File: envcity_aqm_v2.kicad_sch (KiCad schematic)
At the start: 127 parts, among them IC1 DS1307ZN+, IC2 DMMT5401-7F, IC3 DMMT5401-7F, IC4 DMMT5401-7-F, IC6 ESP32-S2-SOLO-N4R2, J1 USB_B_Micro, J12 Conn_01x06_Male, J13 Conn_01x06_Male, J14 Conn_01x08_Pin, J15 Conn_01x02_Male, J16 Conn_01x02_Male, J2 Screw_Terminal_01x02, J3 Screw_Terminal_01x02, J6 Conn_01x04_Male, J7 Conn_01x06_Pin, J8 503398-1892, Q1 DMG2301L / DMP2045U, Q2 DMG2301L / DMP2045U, Q3 DMG2301L, Q4 DMG2301L, Q5 DMG2301L / DMP2045U, Q6 DMG2301L, Q7 DMN10H220L, Q8 DMN10H220L, SW1 BOOT, SW1 RESET, U1 TP4056, U10 RFM95W-915S2, U11 ADS1115IDGS, U2 USBLC6-2SC6, U3 MT3608, U5 LM2596S-5, U6 AP2112K-3.3, U7 DHT11, U8 AP2112K-3.3, U9 74HC4067DB, Y2 AB26TRB

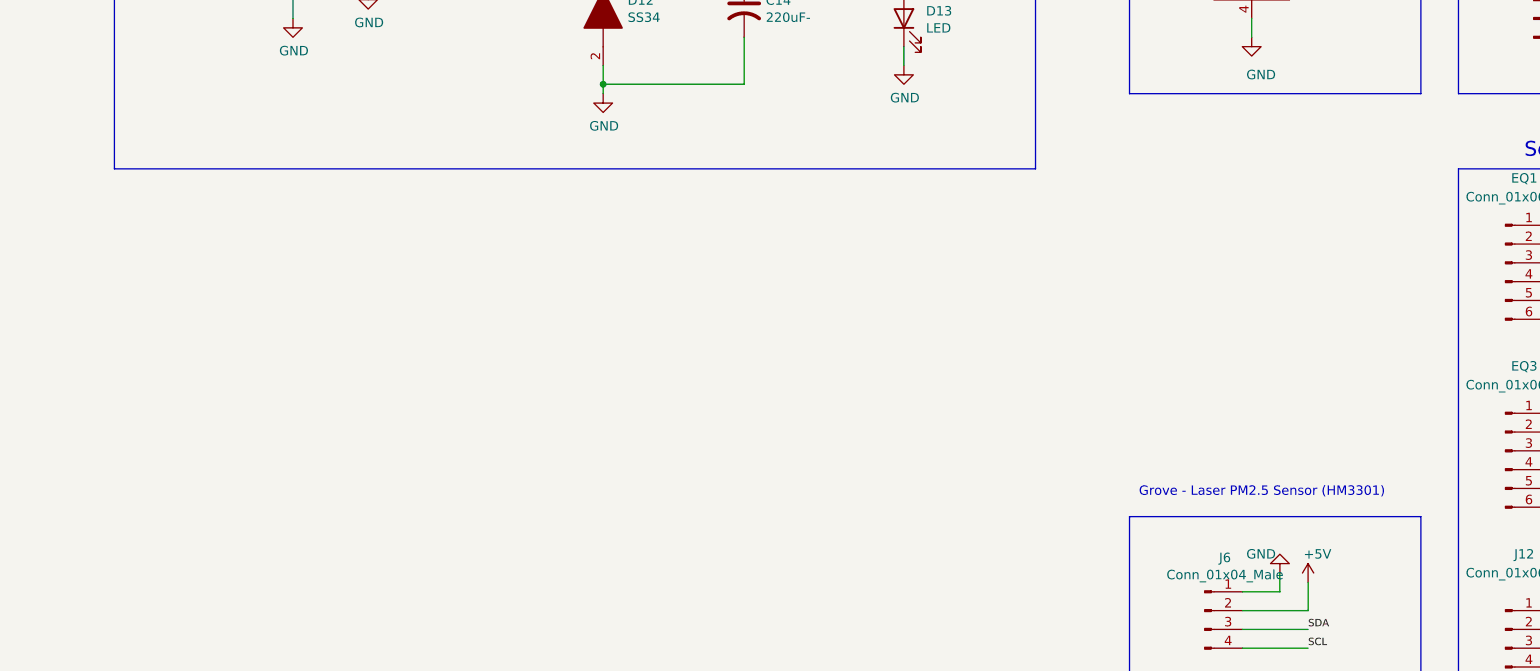
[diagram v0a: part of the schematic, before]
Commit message: board ok. Add tps54202
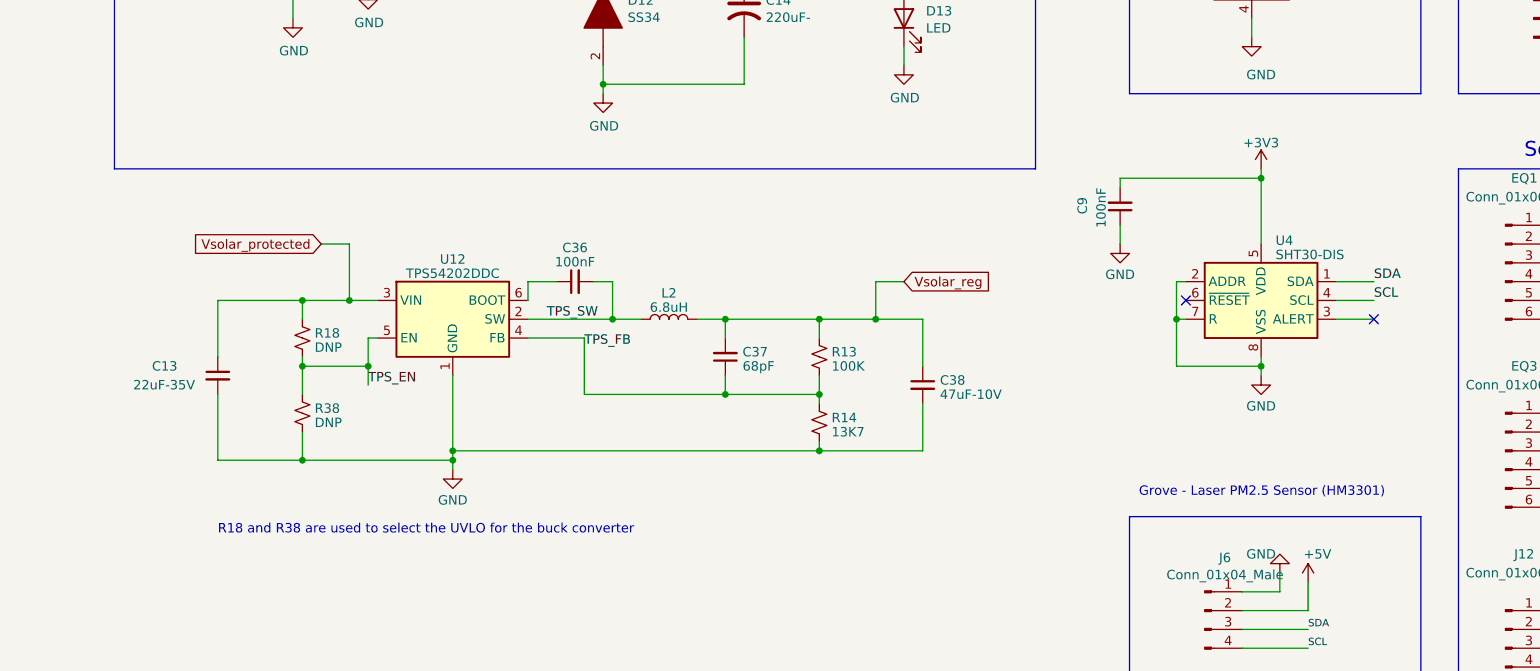
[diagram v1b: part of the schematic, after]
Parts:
- added C13: 22uF-35V, Capacitor_SMD:C_1206_3216Metric, symbol Device:C_Small
- added C36: 100nF, Capacitor_SMD:C_0805_2012Metric, symbol Device:C_Small
- added C37: 68pF, Capacitor_SMD:C_0402_1005Metric, symbol Device:C_Small
- added C38: 47uF-10V, Capacitor_SMD:C_1206_3216Metric, symbol Device:C_Small
- added C9: 100nF, Capacitor_SMD:C_0603_1608Metric, symbol Device:C_Small
- added L2: 6.8uH, Inductor_SMD:L_Coilcraft_XAL4030-XXX, symbol Device:L
- added R13: 100K, Resistor_SMD:R_0402_1005Metric, symbol Device:R_Small_US
- added R14: 13K7, Resistor_SMD:R_0402_1005Metric, symbol Device:R_Small_US
- added R18, R38: DNP, Capacitor_SMD:C_0603_1608Metric_Pad1.08x0.95mm_HandSolder, symbol Device:R_Small_US
- added U12: TPS54202DDC, Package_TO_SOT_SMD:SOT-23-6, symbol Regulator_Switching:TPS54202DDC
- added U4: SHT30-DIS, Sensor_Humidity:Sensirion_DFN-8-1EP_2.5x2.5mm_P0.5mm_EP1.1x1.7mm, symbol Sensor_Humidity:SHT30-DIS
- C28: footprint Capacitor_SMD:C_0805_2012Metric -> Capacitor_SMD:C_0603_1608Metric
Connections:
- net +3V3: now also C9.2, U4.5 (VDD)
- net GND: now also C13.2, C38.2, C9.1, R14.2, R38.2, U12.1 (GND), U4.2 (ADDR), U4.7 (R), U4.8 (VSS), U4.9 (VSS)
- net SCL: now also U4.4 (SCL)
- net SDA: now also U4.1 (SDA)
- net Vsolar_protected: now also C13.1, R18.1, U12.3 (VIN)
- net Vsolar_reg: now also C37.2, C38.1, L2.2, R13.1
- new net: C36.1, U12.6 (BOOT)
- new net TPS_EN: R18.2, R38.1, U12.5 (EN)
- new net TPS_FB: C37.1, R13.2, R14.1, U12.4 (FB)
- new net TPS_SW: C36.2, L2.1, U12.2 (SW)
- no-connect marks 19 -> 21
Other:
- note added: "R18 and R38 are used to select the UVLO for the buck converter"

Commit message: add novo conversor
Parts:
- removed C10: 680uF - Tant, Capacitor_Tantalum_SMD:CP_EIA-7343-15_Kemet-W_Pad2.25x2.55mm_HandSolder, symbol envcity_aqm_v2-rescue:CP1-Device
- removed C14: 220uF-, Capacitor_Tantalum_SMD:CP_EIA-7343-15_Kemet-W_Pad2.25x2.55mm_HandSolder, symbol envcity_aqm_v2-rescue:CP1-Device
- removed D12: SS34, Diode_SMD:D_SMB, symbol envcity_aqm_v2-rescue:SS34-SamacSys_Parts
- removed L3: FAUL0630-330MT, FDSD0630-H-1R0M_P3:IND_FDSD0630-H-1R0M=P3, symbol Device:L
- removed U5: LM2596S-5, Package_TO_SOT_SMD:TO-263-5_TabPin3, symbol Regulator_Switching:LM2596S-5
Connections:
- net TPS_BOOT: now reaches C36.1, U12.6 (BOOT)
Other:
- note added: "Design made by WEBENCH Power Designer: Vin: 7 - 22V Vout 5V @ 1.2A Temp: 45ºC"
- moved on the sheet: C11, C12, C13, C15, C16, C22, C23, C24, C36, C37, C38, C8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

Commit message: add gerber. corrige pcb
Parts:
- BT1: value Battery_Cell -> CR2032-BS-6-1; LCSC Part# (none) -> C70377
- H1, H2, H3, H4: now left out of the parts list
- J8: JLCPCB Part # (none) -> C428492
- L2: value 6.8uH -> SRP5030T-100M; footprint Inductor_SMD:L_Coilcraft_XAL4030-XXX -> Inductor_SMD:L_Bourns_SRP5030T; LCSC Part# (none) -> C189932; Part # XAL4030-682MEB -> SRP5030T-100M
- Q1, Q2, Q5: value DMG2301L / DMP2045U -> DMP2045U-7; LCSC Part# (none) -> C459541
- Q3, Q4, Q6: value DMG2301L -> DMP2045U-7; LCSC Part# (none) -> C459541
- SW1: JLCPCB Part#  (none) -> C221897
- SW1: JLCPCB Part# (none) -> C221897
- Y2: value AB26TRB -> FC-135R; footprint AB26TRB-32.768KHZ-T:XTAL_AB26TRB-32.768KHZ-T -> Crystal:Crystal_SMD_3215-2Pin_3.2x1.5mm; JLCPCB Part # (none) -> C1987155; MANUFACTURER Abracon -> (none); MAXIMUM_PACKAGE_HEIGHT 2 mm -> (none); PARTREV 10-1-19 -> (none); SNAPEDA_PN AB26TRB-32.768KHZ-T -> (none); STANDARD Manufacturer Recommendations -> (none)
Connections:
- net CRYSTAL+: now reaches IC1.1 (X1), Y2.1
- net CRYSTAL-: now reaches IC1.2 (X2), Y2.2
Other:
- note added: "Crystal Specifications f = 32.768 KHz ESR: 45k Cl: 12.5 pF"
- note removed: "Crystal Specifications f = 32,768 KHz ESR: 45k Cl: 12.5 pF"
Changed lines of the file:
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@@
     (effects (font (size 1.27 1.27)) (justify left bottom))
   )
-  (text "Crystal Specifications\n\nf = 32,768 KHz\nESR: 45k\nCl: 12.5 pF"
+  (text "Crystal Specifications\n\nf = 32.768 KHz\nESR: 45k\nCl: 12.5 pF"
     (at 19.05 276.86 0)
     (effects (font (size 1.27 1.27)) (justify left bottom))
@@
     (effects (font (size 1.27 1.27)) (justify left bottom))
   )
+  (label "CRYSTAL-" (at 38.1 288.29 0) (fields_autoplaced)
+    (effects (font (size 1.27 1.27)) (justify left bottom))
+  )
   (label "I2" (at 468.63 50.8 0) (fields_autoplaced)
     (effects (font (size 1.27 1.27)) (justify left bottom))
@@
     (effects (font (size 1.27 1.27)) (justify left bottom))
   )
+  (label "CRYSTAL+" (at 38.1 276.86 0) (fields_autoplaced)
+    (effects (font (size 1.27 1.27)) (justify left bottom))
+  )
   (label "SD_MOSI" (at 49.53 346.71 180) (fields_autoplaced)
     (effects (font (size 1.27 1.27)) (justify right bottom))
@@
       (effects (font (size 1.27 1.27)))
     )
-    (property "Value" "DMG2301L / DMP2045U" (at 337.82 68.326 90)
+    (property "Value" "DMP2045U-7" (at 337.82 68.326 90)
       (effects (font (size 1.27 1.27)))
     )
@@
       (effects (font (size 1.27 1.27)) (justify left) hide)
     )
+    (property "LCSC Part#" "C459541" (at 337.82 59.69 90)
+      (effects (font (size 1.27 1.27)) hide)
+    )
     (pin "1")
     (pin "2")
@@
       (effects (font (size 1.27 1.27)))
     )
-    (property "Value" "DMG2301L / DMP2045U" (at 107.95 126.9746 90)
+    (property "Value" "DMP2045U-7" (at 107.95 126.9746 90)
       (effects (font (size 1.27 1.27)))
     )
@@
       (effects (font (size 1.27 1.27)) (justify left) hide)
     )
+    (property "LCSC Part#" "C459541" (at 107.95 133.35 90)
+      (effects (font (size 1.27 1.27)) hide)
+    )
     (pin "1")
     (pin "2")
@@
       (effects (font (size 1.27 1.27)) (justify left))
     )
-    (property "Value" "Battery_Cell" (at 24.13 295.91 0)
+    (property "Value" "CR2032-BS-6-1" (at 24.13 295.91 0)
       (effects (font (size 1.27 1.27)) (justify left))
     )
@@
       (effects (font (size 1.27 1.27)) hide)
     )
+    (property "LCSC Part#" "C70377" (at 38.1 295.91 0)
+      (effects (font (size 1.27 1.27)) hide)
+    )
     (pin "1")
     (pin "2")
@@
       (effects (font (size 1.27 1.27)))
     )
-    (property "Value" "DMG2301L" (at 242.57 34.2646 90)
+    (property "Value" "DMP2045U-7" (at 242.57 34.2646 90)
       (effects (font (size 1.27 1.27)))
     )
@@
       (effects (font (size 1.27 1.27)) (justify left) hide)
     )
+    (property "LCSC Part#" "C459541" (at 242.57 40.64 90)
+      (effects (font (size 1.27 1.27)) hide)
+    )
     (pin "1")
     (pin "2")
@@
       (effects (font (size 1.27 1.27)))
     )
-    (property "Value" "DMG2301L" (at 288.29 43.1546 90)
+    (property "Value" "DMP2045U-7" (at 288.29 43.1546 90)
       (effects (font (size 1.27 1.27)))
     )
@@
       (effects (font (size 1.27 1.27)) (justify left) hide)
     )
+    (property "LCSC Part#" "C459541" (at 288.29 49.53 90)
+      (effects (font (size 1.27 1.27)) hide)
+    )
     (pin "1")
     (pin "2")
@@
       (effects (font (size 1.27 1.27)))
     )
-    (property "Value" "DMG2301L" (at 341.63 77.4446 90)
+    (property "Value" "DMP2045U-7" (at 341.63 77.4446 90)
       (effects (font (size 1.27 1.27)))
     )
@@
       (effects (font (size 1.27 1.27)) (justify left) hide)
     )
+    (property "LCSC Part#" "C459541" (at 341.63 83.82 90)
+      (effects (font (size 1.27 1.27)) hide)
+    )
     (pin "1")
     (pin "2")
@@
   )
   (symbol (lib_id "Mechanical:MountingHole") (at 30.48 388.62 0) (unit 1)
-    (in_bom yes) (on_board yes) (dnp no)
+    (in_bom no) (on_board yes) (dnp no)
     (property "Reference" "H1" (at 33.02 387.4516 0)
       (effects (font (size 1.27 1.27)) (justify left))
@@
   )
   (symbol (lib_id "Mechanical:MountingHole") (at 30.48 394.97 0) (unit 1)
-    (in_bom yes) (on_board yes) (dnp no)
+    (in_bom no) (on_board yes) (dnp no)
     (property "Reference" "H2" (at 33.02 393.8016 0)
       (effects (font (size 1.27 1.27)) (justify left))
@@
   )
   (symbol (lib_id "Mechanical:MountingHole") (at 52.07 388.62 0) (unit 1)
-    (in_bom yes) (on_board yes) (dnp no)
+    (in_bom no) (on_board yes) (dnp no)
     (property "Reference" "H3" (at 54.61 387.4516 0)
       (effects (font (size 1.27 1.27)) (justify left))
@@
   )
   (symbol (lib_id "Mechanical:MountingHole") (at 52.07 394.97 0) (unit 1)
-    (in_bom yes) (on_board yes) (dnp no)
+    (in_bom no) (on_board yes) (dnp no)
     (property "Reference" "H4" (at 54.61 393.8016 0)
       (effects (font (size 1.27 1.27)) (justify left))
@@
       (effects (font (size 1.27 1.27)))
     )
-    (property "Value" "DMG2301L / DMP2045U" (at 107.95 78.7146 90)
+    (property "Value" "DMP2045U-7" (at 107.95 78.7146 90)
       (effects (font (size 1.27 1.27)))
     )
@@
       (effects (font (size 1.27 1.27)) (justify left) hide)
     )
+    (property "LCSC Part#" "C459541" (at 107.95 85.09 90)
+      (effects (font (size 1.27 1.27)) hide)
+    )
     (pin "1")
     (pin "2")
@@
       (effects (font (size 1.27 1.27)) hide)
     )
+    (property "JLCPCB Part #" "C428492" (at 53.34 341.63 0)
+      (effects (font (size 1.27 1.27)) hide)
+    )
     (pin "1")
     (pin "10")
@@
   )
   (symbol (lib_id "Device:L") (at 204.47 182.88 90) (unit 1)
-    (in_bom yes) (on_board yes) (dnp no) (fields_autoplaced)
-    (property "Reference" "L2" (at 204.47 179.3647 90)
+    (in_bom yes) (on_board yes) (dnp no)
+    (property "Reference" "L2" (at 204.47 177.8 90)
       (effects (font (size 1.27 1.27)))
     )
-    (property "Value" "6.8uH" (at 204.47 181.2857 90)
+    (property "Value" "SRP5030T-100M" (at 205.74 180.34 90)
       (effects (font (size 1.27 1.27)))
     )
-    (property "Footprint" "Inductor_SMD:L_Coilcraft_XAL4030-XXX" (at 204.47 182.88 0)
+    (property "Footprint" "Inductor_SMD:L_Bourns_SRP5030T" (at 204.47 182.88 0)
       (effects (font (size 1.27 1.27)) hide)
     )
@@
       (effects (font (size 1.27 1.27)) hide)
     )
-    (property "Part #" "XAL4030-682MEB" (at 204.47 182.88 90)
+    (property "Part #" "SRP5030T-100M" (at 204.47 182.88 90)
+      (effects (font (size 1.27 1.27)) hide)
+    )
+    (property "LCSC Part#" "C189932" (at 204.47 182.88 90)
       (effects (font (size 1.27 1.27)) hide)
     )
@@
       (effects (font (size 1.27 1.27)) hide)
     )
+    (property "JLCPCB Part# " "C221897" (at 506.73 144.78 0)
+      (effects (font (size 1.27 1.27)) hide)
+    )
     (pin "1")
     (pin "2")
@@
       (effects (font (size 1.27 1.27)) (justify left))
     )
-    (property "Value" "AB26TRB" (at 30.48 283.845 90)
+    (property "Value" "FC-135R" (at 30.48 283.845 90)
       (effects (font (size 1.27 1.27)) (justify left))
     )
-    (property "Footprint" "AB26TRB-32.768KHZ-T:XTAL_AB26TRB-32.768KHZ-T" (at 34.29 281.94 0)
+    (property "Footprint" "Crystal:Crystal_SMD_3215-2Pin_3.2x1.5mm" (at 34.29 281.94 0)
       (effects (font (size 1.27 1.27)) (justify bottom) hide)
     )
@@
       (effects (font (size 1.27 1.27)) hide)
     )
-    (property "PARTREV" "10-1-19" (at 34.29 281.94 0)
-      (effects (font (size 1.27 1.27)) (justify bottom) hide)
-    )
-    (property "STANDARD" "Manufacturer Recommendations" (at 34.29 281.94 0)
-      (effects (font (size 1.27 1.27)) (justify bottom) hide)
-    )
-    (property "SNAPEDA_PN" "AB26TRB-32.768KHZ-T" (at 34.29 281.94 0)
-      (effects (font (size 1.27 1.27)) (justify bottom) hide)
-    )
-    (property "MAXIMUM_PACKAGE_HEIGHT" "2 mm" (at 34.29 281.94 0)
-      (effects (font (size 1.27 1.27)) (justify bottom) hide)
-    )
-    (property "MANUFACTURER" "Abracon" (at 34.29 281.94 0)
-      (effects (font (size 1.27 1.27)) (justify bottom) hide)
+    (property "JLCPCB Part #" "C1987155" (at 34.29 281.94 90)
+      (effects (font (size 1.27 1.27)) hide)
     )
     (pin "1")
@@
       (effects (font (size 1.27 1.27)) hide)
     )
+    (property "JLCPCB Part#" "C221897" (at 439.42 154.94 0)
+      (effects (font (size 1.27 1.27)) hide)
+    )

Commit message: altera componentes
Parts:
- AE1: LCSC Part # (none) -> C434806
- D1: value D_TVS_ALT -> HESD5Z24; LCSC Part # (none) -> C3002989
- D2: value D_TVS_ALT -> VESD05A1; LCSC Part # (none) -> C1974922
- EQ3: LCSC # (none) -> C504992
- J14: JLCPCB Part # (none) -> C240845
- J15: LCSC Part # (none) -> C505162; Mfr. Part # (none) -> 22112022
- J2: LCSC Part # (none) -> C3029316
- J6: LCSC Part # (none) -> C2764213
- U10: value RFM95W-915S2 -> RFM95W-915; AlternativeValue (none) -> DreamLNK DL-RFM95-915M; LCSC # (none) -> C2844473
- Y2: LCSC Part # (none) -> C179645
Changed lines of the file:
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@@
       (effects (font (size 1.27 1.27)) hide)
     )
+    (property "LCSC #" "C504992" (at 325.12 252.73 0)
+      (effects (font (size 1.27 1.27)) hide)
+    )
     (pin "1")
     (pin "2")
@@
       (effects (font (size 1.27 1.27)) (justify left))
     )
-    (property "Value" "D_TVS_ALT" (at 92.1766 138.303 90)
+    (property "Value" "VESD05A1" (at 92.1766 138.303 90)
       (effects (font (size 1.27 1.27)) (justify left))
     )
@@
       (effects (font (size 1.27 1.27)) hide)
     )
+    (property "LCSC Part #" "C1974922" (at 90.17 137.16 90)
+      (effects (font (size 1.27 1.27)) hide)
+    )
     (pin "1")
     (pin "2")
@@
       (effects (font (size 1.27 1.27)) hide)
     )
+    (property "Mfr. Part #" "22112022" (at 447.04 327.66 0)
+      (effects (font (size 1.27 1.27)) hide)
+    )
+    (property "LCSC Part #" "C505162" (at 447.04 327.66 0)
+      (effects (font (size 1.27 1.27)) hide)
+    )
     (pin "1")
     (pin "2")
@@
       (effects (font (size 1.27 1.27)) hide)
     )
+    (property "LCSC Part #" "C3029316" (at 72.39 82.55 0)
+      (effects (font (size 1.27 1.27)) hide)
+    )
     (pin "1")
     (pin "2")
@@
       (effects (font (size 1.27 1.27)) hide)
     )
+    (property "LCSC Part #" "C2764213" (at 284.48 274.32 0)
+      (effects (font (size 1.27 1.27)) hide)
+    )
     (pin "1")
     (pin "2")
@@
       (effects (font (size 1.27 1.27)) (justify left))
     )
-    (property "Value" "D_TVS_ALT" (at 92.1766 90.043 90)
+    (property "Value" "HESD5Z24" (at 92.1766 90.043 90)
       (effects (font (size 1.27 1.27)) (justify left))
     )
@@
       (effects (font (size 1.27 1.27)) hide)
     )
+    (property "LCSC Part #" "C3002989" (at 90.17 88.9 90)
+      (effects (font (size 1.27 1.27)) hide)
+    )
     (pin "1")
     (pin "2")
@@
       (effects (font (size 1.27 1.27)) hide)
     )
+    (property "LCSC Part #" "C434806" (at 499.11 260.35 0)
+      (effects (font (size 1.27 1.27)) hide)
+    )
     (pin "1")
     (instances
@@
       (effects (font (size 1.27 1.27)) (justify left))
     )
-    (property "Value" "RFM95W-915S2" (at 475.6659 261.8011 0)
+    (property "Value" "RFM95W-915" (at 475.6659 261.8011 0)
       (effects (font (size 1.27 1.27)) (justify left))
     )
@@
       (effects (font (size 1.27 1.27)) hide)
     )
+    (property "LCSC #" "C2844473" (at 473.71 273.05 0)
+      (effects (font (size 1.27 1.27)) hide)
+    )
+    (property "AlternativeValue" "DreamLNK DL-RFM95-915M" (at 473.71 273.05 0)
+      (effects (font (size 1.27 1.27)) hide)
+    )
     (pin "1")
     (pin "10")
@@
       (effects (font (size 1.27 1.27)) hide)
     )
+    (property "JLCPCB Part #" "C240845" (at 328.93 186.69 0)
+      (effects (font (size 1.27 1.27)) hide)
+    )
     (pin "1")
     (pin "2")
@@
       (effects (font (size 1.27 1.27)) hide)
     )
+    (property "LCSC Part #" "C179645" (at 34.29 281.94 90)
+      (effects (font (size 1.27 1.27)) hide)
+    )
